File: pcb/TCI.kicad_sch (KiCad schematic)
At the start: 16 parts, among them IC4 UCC27624QDRQ1, Q10 AO3400A, Q2 IRLIZ44N, Q4 STGB20M65DF2

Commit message: added ideal maximum board size
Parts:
- Q4: footprint SamacSys_Parts:STGB20M65DF2 -> Package_TO_SOT_SMD:TO-263-2
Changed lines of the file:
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@@
 			)
 		)
-		(property "Footprint" "SamacSys_Parts:STGB20M65DF2"
+		(property "Footprint" "Package_TO_SOT_SMD:TO-263-2"
 			(at 118.11 173.99 0)
 			(effects

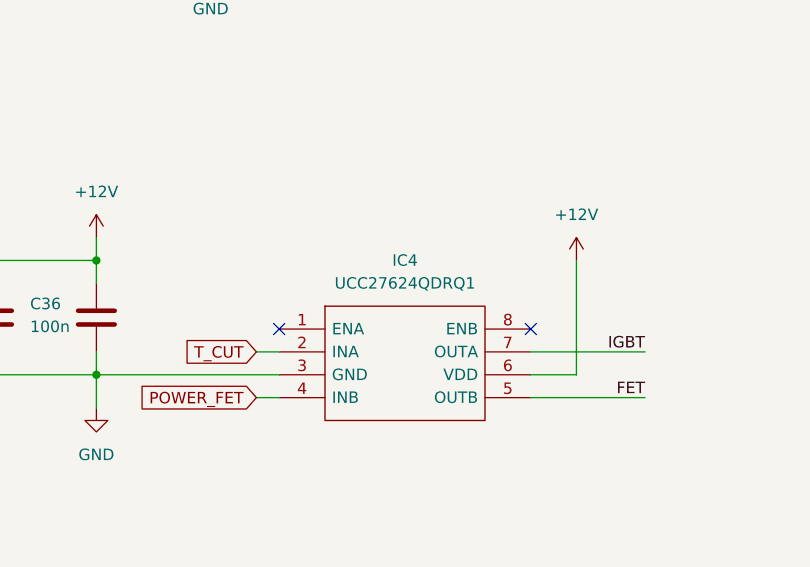
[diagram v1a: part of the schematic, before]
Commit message: revision 2.0: added LC Vbatt filtering and changed Pmos protection to be a schttoky
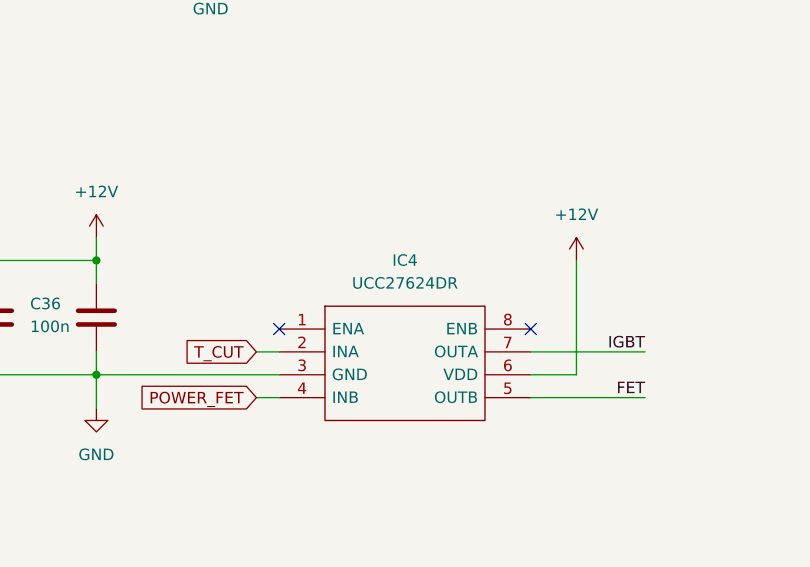
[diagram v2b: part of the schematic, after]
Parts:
- IC4: value UCC27624QDRQ1 -> UCC27624DR
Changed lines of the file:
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@@
 			)
 		)
-		(property "Value" "UCC27624QDRQ1"
+		(property "Value" "UCC27624DR"
 			(at 78.74 105.41 0)
 			(effects

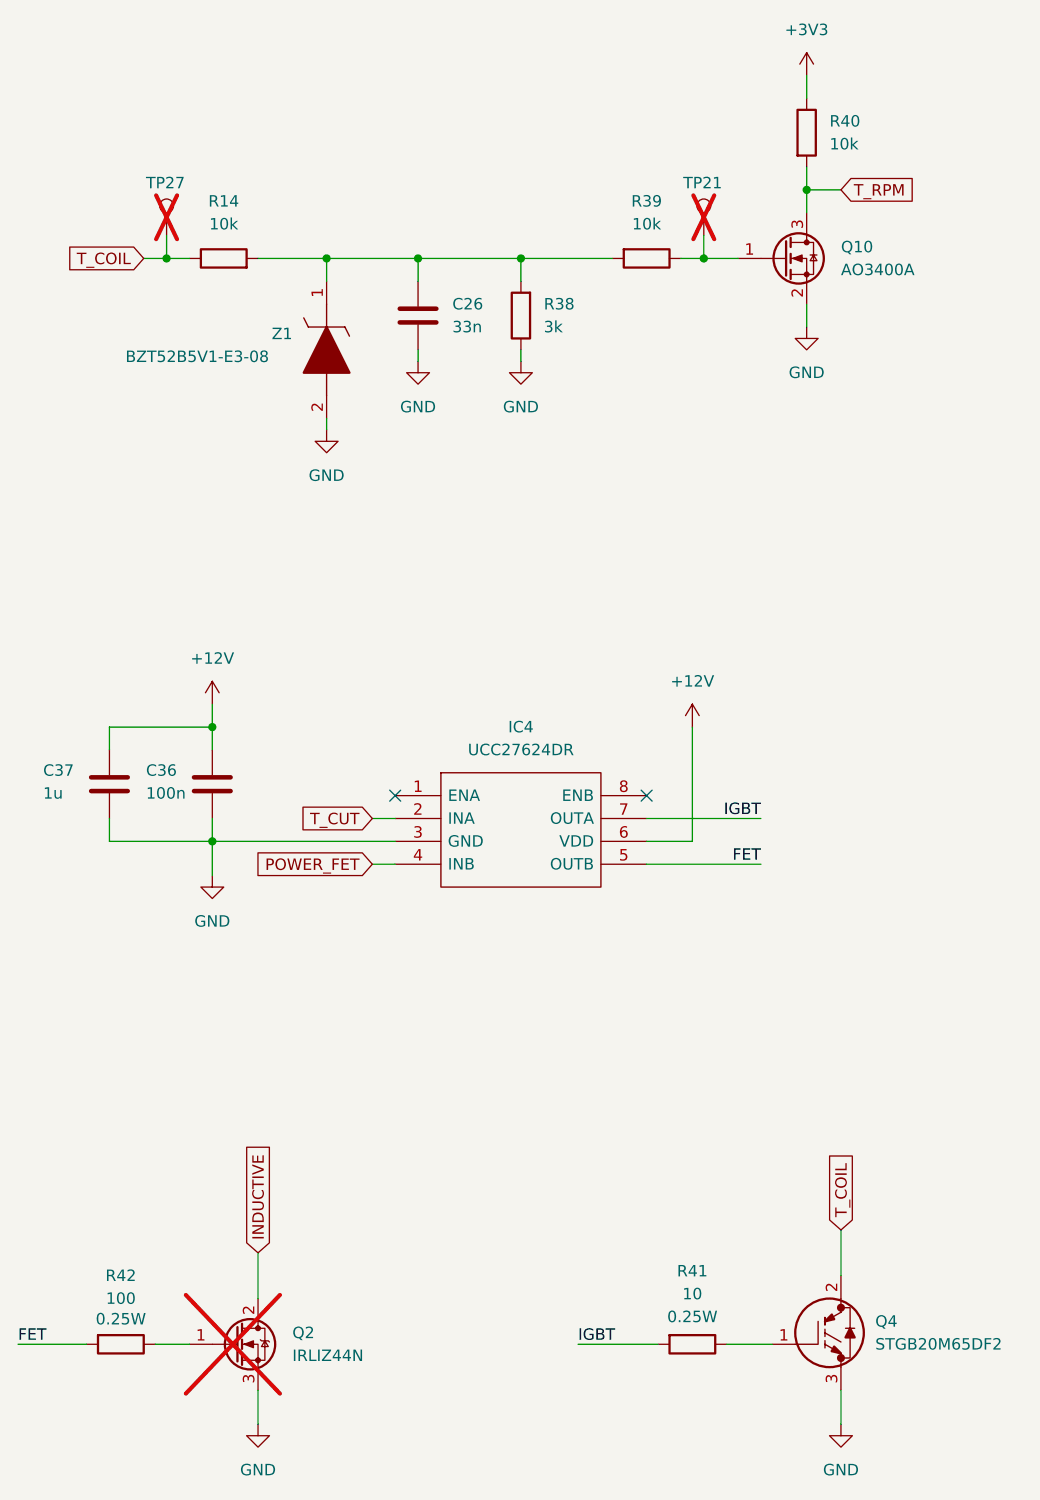
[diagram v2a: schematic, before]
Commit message: revision 2.0: changed components numeration
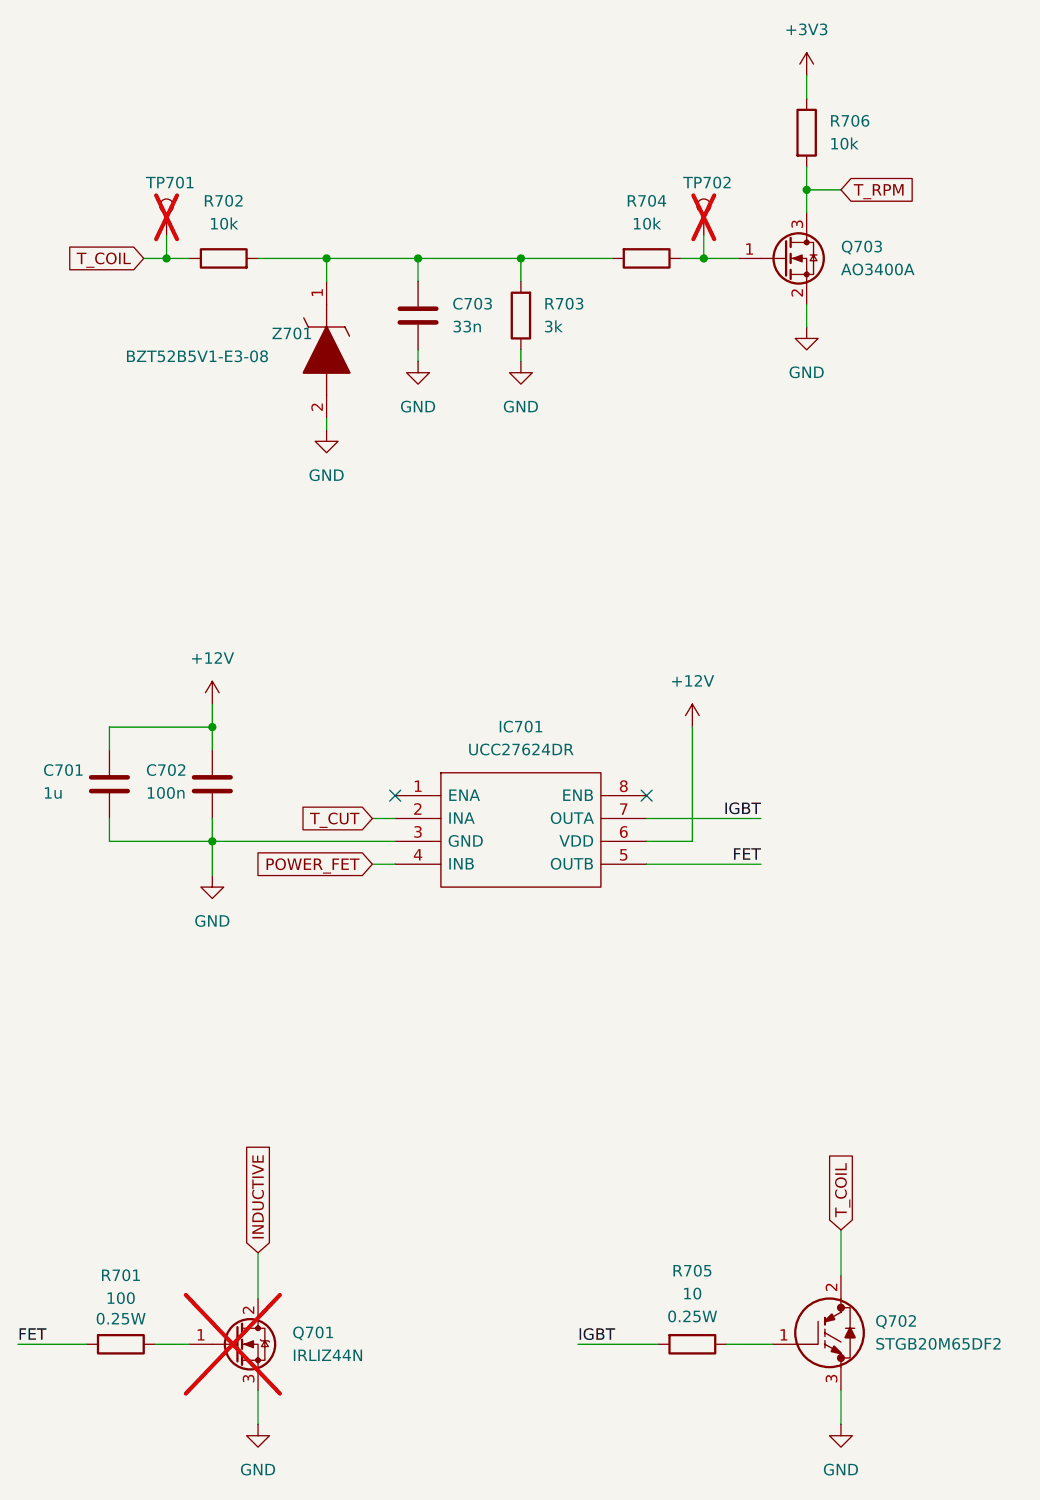
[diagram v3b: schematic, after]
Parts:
- renumbered C37 to C701, C36 to C702, C26 to C703, IC4 to IC701, Q2 to Q701, Q4 to Q702, Q10 to Q703, R42 to R701, R14 to R702, R38 to R703, R39 to R704, R41 to R705, R40 to R706, TP27 to TP701, TP21 to TP702, Z1 to Z701
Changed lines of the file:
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@@
 		(dnp no)
 		(fields_autoplaced yes)
-		(property "Reference" "#PWR040"
+		(property "Reference" "#PWR0706"
 			(at 78.74 68.58 0)
 			(effects
@@
 			(project "ecu-dev-board"
 				(path "/38d4df77-b5a0-4642-8410-8b13c21c2c3b/1f135221-d921-46ea-b769-b97fce3b730c"
-					(reference "#PWR040")
+					(reference "#PWR0706")
 					(unit 1)
 				)
@@
 		(on_board yes)
 		(dnp no)
-		(property "Reference" "Z1"
+		(property "Reference" "Z701"
 			(at 51.054 59.182 90)
 			(effects
@@
 			(project ""
 				(path "/38d4df77-b5a0-4642-8410-8b13c21c2c3b/1f135221-d921-46ea-b769-b97fce3b730c"
-					(reference "Z1")
+					(reference "Z701")
 					(unit 1)
 				)
@@
 		(dnp no)
 		(fields_autoplaced yes)
-		(property "Reference" "#PWR045"
+		(property "Reference" "#PWR0701"
 			(at 44.45 104.14 0)
 			(effects
@@
 			(project "ecu-dev-board"
 				(path "/38d4df77-b5a0-4642-8410-8b13c21c2c3b/1f135221-d921-46ea-b769-b97fce3b730c"
-					(reference "#PWR045")
+					(reference "#PWR0701")
 					(unit 1)
 				)
@@
 		(dnp no)
 		(fields_autoplaced yes)
-		(property "Reference" "C26"
+		(property "Reference" "C703"
 			(at 71.12 55.8799 0)
 			(effects
@@
 			(project ""
 				(path "/38d4df77-b5a0-4642-8410-8b13c21c2c3b/1f135221-d921-46ea-b769-b97fce3b730c"
-					(reference "C26")
+					(reference "C703")
 					(unit 1)
 				)
@@
 		(on_board yes)
 		(dnp no)
-		(property "Reference" "C36"
+		(property "Reference" "C702"
 			(at 37.084 107.696 0)
 			(effects
@@
 			(project "ecu-dev-board"
 				(path "/38d4df77-b5a0-4642-8410-8b13c21c2c3b/1f135221-d921-46ea-b769-b97fce3b730c"
-					(reference "C36")
+					(reference "C702")
 					(unit 1)
 				)
@@
 		(on_board yes)
 		(dnp yes)
-		(property "Reference" "TP21"
+		(property "Reference" "TP702"
 			(at 96.774 42.418 0)
 			(effects
@@
 			(project "ecu-dev-board"
 				(path "/38d4df77-b5a0-4642-8410-8b13c21c2c3b/1f135221-d921-46ea-b769-b97fce3b730c"
-					(reference "TP21")
+					(reference "TP702")
 					(unit 1)
 				)
@@
 		(on_board yes)
 		(dnp yes)
-		(property "Reference" "TP27"
+		(property "Reference" "TP701"
 			(at 37.084 42.418 0)
 			(effects
@@
 			(project "ecu-dev-board"
 				(path "/38d4df77-b5a0-4642-8410-8b13c21c2c3b/1f135221-d921-46ea-b769-b97fce3b730c"
-					(reference "TP27")
+					(reference "TP701")
 					(unit 1)
 				)
@@
 		(dnp yes)
 		(fields_autoplaced yes)
-		(property "Reference" "Q2"
+		(property "Reference" "Q701"
 			(at 53.34 170.1799 0)
 			(effects
@@
 			(project ""
 				(path "/38d4df77-b5a0-4642-8410-8b13c21c2c3b/1f135221-d921-46ea-b769-b97fce3b730c"
-					(reference "Q2")
+					(reference "Q701")
 					(unit 1)
 				)
@@
 		(on_board yes)
 		(dnp no)
-		(property "Reference" "C37"
+		(property "Reference" "C701"
 			(at 25.654 107.696 0)
 			(effects
@@
 			(project "ecu-dev-board"
 				(path "/38d4df77-b5a0-4642-8410-8b13c21c2c3b/1f135221-d921-46ea-b769-b97fce3b730c"
-					(reference "C37")
+					(reference "C701")
 					(unit 1)
 				)
@@
 		(dnp no)
 		(fields_autoplaced yes)
-		(property "Reference" "R38"
+		(property "Reference" "R703"
 			(at 81.28 55.8799 0)
 			(effects
@@
 			(project "ecu-dev-board"
 				(path "/38d4df77-b5a0-4642-8410-8b13c21c2c3b/1f135221-d921-46ea-b769-b97fce3b730c"
-					(reference "R38")
+					(reference "R703")
 					(unit 1)
 				)
@@
 		(dnp no)
 		(fields_autoplaced yes)
-		(property "Reference" "#PWR042"
+		(property "Reference" "#PWR0708"
 			(at 110.49 34.29 0)
 			(effects
@@
 			(project "ecu-dev-board"
 				(path "/38d4df77-b5a0-4642-8410-8b13c21c2c3b/1f135221-d921-46ea-b769-b97fce3b730c"
-					(reference "#PWR042")
+					(reference "#PWR0708")
 					(unit 1)
 				)
@@
 		(dnp no)
 		(fields_autoplaced yes)
-		(property "Reference" "#PWR047"
+		(property "Reference" "#PWR0703"
 			(at 49.53 186.69 0)
 			(effects
@@
 			(project "ecu-dev-board"
 				(path "/38d4df77-b5a0-4642-8410-8b13c21c2c3b/1f135221-d921-46ea-b769-b97fce3b730c"
-					(reference "#PWR047")
+					(reference "#PWR0703")
 					(unit 1)
 				)
@@
 		(dnp no)
 		(fields_autoplaced yes)
-		(property "Reference" "IC4"
+		(property "Reference" "IC701"
 			(at 78.74 102.87 0)
 			(effects
@@
 			(project ""
 				(path "/38d4df77-b5a0-4642-8410-8b13c21c2c3b/1f135221-d921-46ea-b769-b97fce3b730c"
-					(reference "IC4")
+					(reference "IC701")
 					(unit 1)
 				)
@@
 		(dnp no)
 		(fields_autoplaced yes)
-		(property "Reference" "#PWR039"
+		(property "Reference" "#PWR0705"
 			(at 67.31 68.58 0)
 			(effects
@@
 			(project ""
 				(path "/38d4df77-b5a0-4642-8410-8b13c21c2c3b/1f135221-d921-46ea-b769-b97fce3b730c"
-					(reference "#PWR039")
+					(reference "#PWR0705")
 					(unit 1)
 				)
@@
 		(on_board yes)
 		(dnp no)
-		(property "Reference" "R42"
+		(property "Reference" "R701"
 			(at 34.29 163.83 90)
 			(effects
@@
 			(project "ecu-dev-board"
 				(path "/38d4df77-b5a0-4642-8410-8b13c21c2c3b/1f135221-d921-46ea-b769-b97fce3b730c"
-					(reference "R42")
+					(reference "R701")
 					(unit 1)
 				)
@@
 		(on_board yes)
 		(dnp no)
-		(property "Reference" "R41"
+		(property "Reference" "R705"
 			(at 97.79 163.322 90)
 			(effects
@@
 			(project "ecu-dev-board"
 				(path "/38d4df77-b5a0-4642-8410-8b13c21c2c3b/1f135221-d921-46ea-b769-b97fce3b730c"
-					(reference "R41")
+					(reference "R705")
 					(unit 1)
 				)
@@
 		(dnp no)
 		(fields_autoplaced yes)
-		(property "Reference" "#PWR082"
+		(property "Reference" "#PWR0709"
 			(at 110.49 64.77 0)
 			(effects
@@
 			(project "ecu-dev-board"
 				(path "/38d4df77-b5a0-4642-8410-8b13c21c2c3b/1f135221-d921-46ea-b769-b97fce3b730c"
-					(reference "#PWR082")
+					(reference "#PWR0709")
 					(unit 1)
 				)
@@
 		(dnp no)
 		(fields_autoplaced yes)
-		(property "Reference" "R40"
+		(property "Reference" "R706"
 			(at 113.03 35.5599 0)
 			(effects
@@
 			(project "ecu-dev-board"
 				(path "/38d4df77-b5a0-4642-8410-8b13c21c2c3b/1f135221-d921-46ea-b769-b97fce3b730c"
-					(reference "R40")
+					(reference "R706")
 					(unit 1)
 				)
@@
 		(dnp no)
 		(fields_autoplaced yes)
-		(property "Reference" "Q10"
+		(property "Reference" "Q703"
 			(at 114.3 49.5299 0)
 			(effects
@@
 			(project ""
 				(path "/38d4df77-b5a0-4642-8410-8b13c21c2c3b/1f135221-d921-46ea-b769-b97fce3b730c"
-					(reference "Q10")
+					(reference "Q703")
 					(unit 1)
 				)
@@
 		(dnp no)
 		(fields_autoplaced yes)
-		(property "Reference" "#PWR044"
+		(property "Reference" "#PWR0707"
 			(at 97.79 106.68 0)
 			(effects
@@
 			(project ""
 				(path "/38d4df77-b5a0-4642-8410-8b13c21c2c3b/1f135221-d921-46ea-b769-b97fce3b730c"
-					(reference "#PWR044")
+					(reference "#PWR0707")
 					(unit 1)
 				)
@@
 		(dnp no)
 		(fields_autoplaced yes)
-		(property "Reference" "#PWR043"
+		(property "Reference" "#PWR0702"
 			(at 44.45 125.73 0)
 			(effects
@@
 			(project "ecu-dev-board"
 				(path "/38d4df77-b5a0-4642-8410-8b13c21c2c3b/1f135221-d921-46ea-b769-b97fce3b730c"
-					(reference "#PWR043")
+					(reference "#PWR0702")
 					(unit 1)
 				)
@@
 		(dnp no)
 		(fields_autoplaced yes)
-		(property "Reference" "R14"
+		(property "Reference" "R702"
 			(at 45.72 44.45 90)
 			(effects
@@
 			(project ""
 				(path "/38d4df77-b5a0-4642-8410-8b13c21c2c3b/1f135221-d921-46ea-b769-b97fce3b730c"
-					(reference "R14")
+					(reference "R702")
 					(unit 1)
 				)
@@
 		(dnp no)
 		(fields_autoplaced yes)
-		(property "Reference" "#PWR041"
+		(property "Reference" "#PWR0704"
 			(at 57.15 76.2 0)
 			(effects
@@
 			(project "ecu-dev-board"
 				(path "/38d4df77-b5a0-4642-8410-8b13c21c2c3b/1f135221-d921-46ea-b769-b97fce3b730c"
-					(reference "#PWR041")
+					(reference "#PWR0704")
 					(unit 1)
 				)
@@
 		(dnp no)
 		(fields_autoplaced yes)
-		(property "Reference" "R39"
+		(property "Reference" "R704"
 			(at 92.71 44.45 90)
 			(effects
@@
 			(project "ecu-dev-board"
 				(path "/38d4df77-b5a0-4642-8410-8b13c21c2c3b/1f135221-d921-46ea-b769-b97fce3b730c"
-					(reference "R39")
+					(reference "R704")
 					(unit 1)
 				)
@@
 		(dnp no)
 		(fields_autoplaced yes)
-		(property "Reference" "#PWR046"
+		(property "Reference" "#PWR0710"
 			(at 114.3 186.69 0)
 			(effects
@@
 			(project "ecu-dev-board"
 				(path "/38d4df77-b5a0-4642-8410-8b13c21c2c3b/1f135221-d921-46ea-b769-b97fce3b730c"
-					(reference "#PWR046")
+					(reference "#PWR0710")
 					(unit 1)
 				)
@@
 		(dnp no)
 		(fields_autoplaced yes)
-		(property "Reference" "Q4"
+		(property "Reference" "Q702"
 			(at 118.11 168.9099 0)
 			(effects
@@
 			(project "ecu-dev-board"
 				(path "/38d4df77-b5a0-4642-8410-8b13c21c2c3b/1f135221-d921-46ea-b769-b97fce3b730c"
-					(reference "Q4")
-					(unit 1)
-				)
+					(reference "Q702")
+					(unit 1)
+				)

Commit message: revision 2.0: changed R and C footprints to 0805 (imperial)
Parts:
- C701, C702, C703: footprint Capacitor_SMD:C_0603_1608Metric -> Capacitor_SMD:C_0805_2012Metric
- R702, R703, R704, R706: footprint Resistor_SMD:R_0603_1608Metric -> Resistor_SMD:R_0805_2012Metric
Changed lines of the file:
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@@
 			)
 		)
-		(property "Footprint" "Capacitor_SMD:C_0603_1608Metric"
+		(property "Footprint" "Capacitor_SMD:C_0805_2012Metric"
 			(at 68.2752 60.96 0)
 			(effects
@@
 			)
 		)
-		(property "Footprint" "Capacitor_SMD:C_0603_1608Metric"
+		(property "Footprint" "Capacitor_SMD:C_0805_2012Metric"
 			(at 45.4152 113.03 0)
 			(effects
@@
 			)
 		)
-		(property "Footprint" "Capacitor_SMD:C_0603_1608Metric"
+		(property "Footprint" "Capacitor_SMD:C_0805_2012Metric"
 			(at 33.9852 113.03 0)
 			(effects
@@
 			)
 		)
-		(property "Footprint" "Resistor_SMD:R_0603_1608Metric"
+		(property "Footprint" "Resistor_SMD:R_0805_2012Metric"
 			(at 80.518 57.15 90)
 			(effects
@@
 			)
 		)
-		(property "Footprint" "Resistor_SMD:R_0603_1608Metric"
+		(property "Footprint" "Resistor_SMD:R_0805_2012Metric"
 			(at 108.712 36.83 90)
 			(effects
@@
 			)
 		)
-		(property "Footprint" "Resistor_SMD:R_0603_1608Metric"
+		(property "Footprint" "Resistor_SMD:R_0805_2012Metric"
 			(at 45.72 52.578 90)
 			(effects
@@
 			)
 		)
-		(property "Footprint" "Resistor_SMD:R_0603_1608Metric"
+		(property "Footprint" "Resistor_SMD:R_0805_2012Metric"
 			(at 92.71 49.022 90)
 			(effects

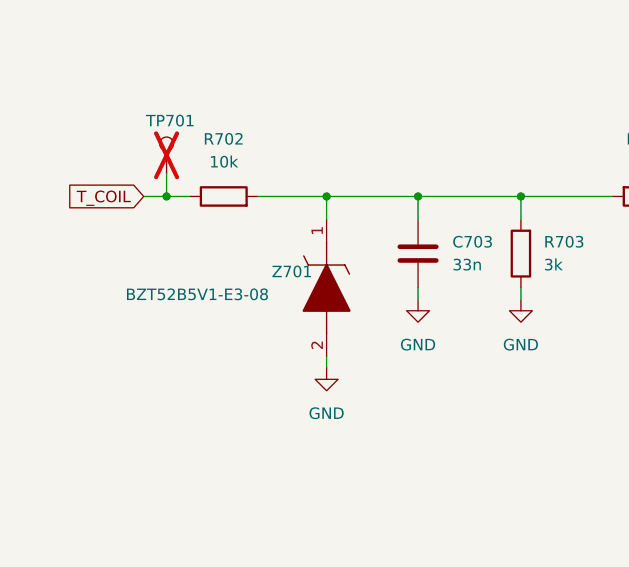
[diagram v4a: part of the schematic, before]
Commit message: removed unnecessary silkscreen designators
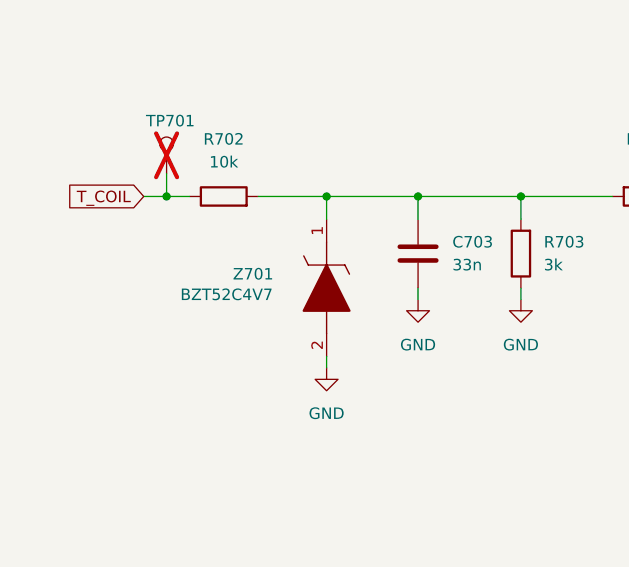
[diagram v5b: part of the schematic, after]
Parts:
- Z701: value BZT52B5V1-E3-08 -> BZT52C4V7
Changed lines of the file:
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@@
 		(dnp no)
 		(property "Reference" "Z701"
-			(at 51.054 59.182 90)
+			(at 46.736 59.436 90)
 			(effects
 				(font
@@
 			)
 		)
-		(property "Value" "BZT52B5V1-E3-08"
-			(at 34.798 61.722 90)
+		(property "Value" "BZT52C4V7"
+			(at 40.894 61.722 90)
 			(effects
 				(font
